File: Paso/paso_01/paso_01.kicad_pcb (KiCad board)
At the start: 2 copper layers, 97.4 x 87.2 mm, 2 parts

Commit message: Some minors update paso
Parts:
- removed the Ref** at (117.0, 110.7)
- added Ref**: Val**, paso_01:Maker_Lugo_100mm_02, F.Cu at (116.3, 122.3)
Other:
- board size 97.4 x 87.2 mm -> 97.4 x 87 mm

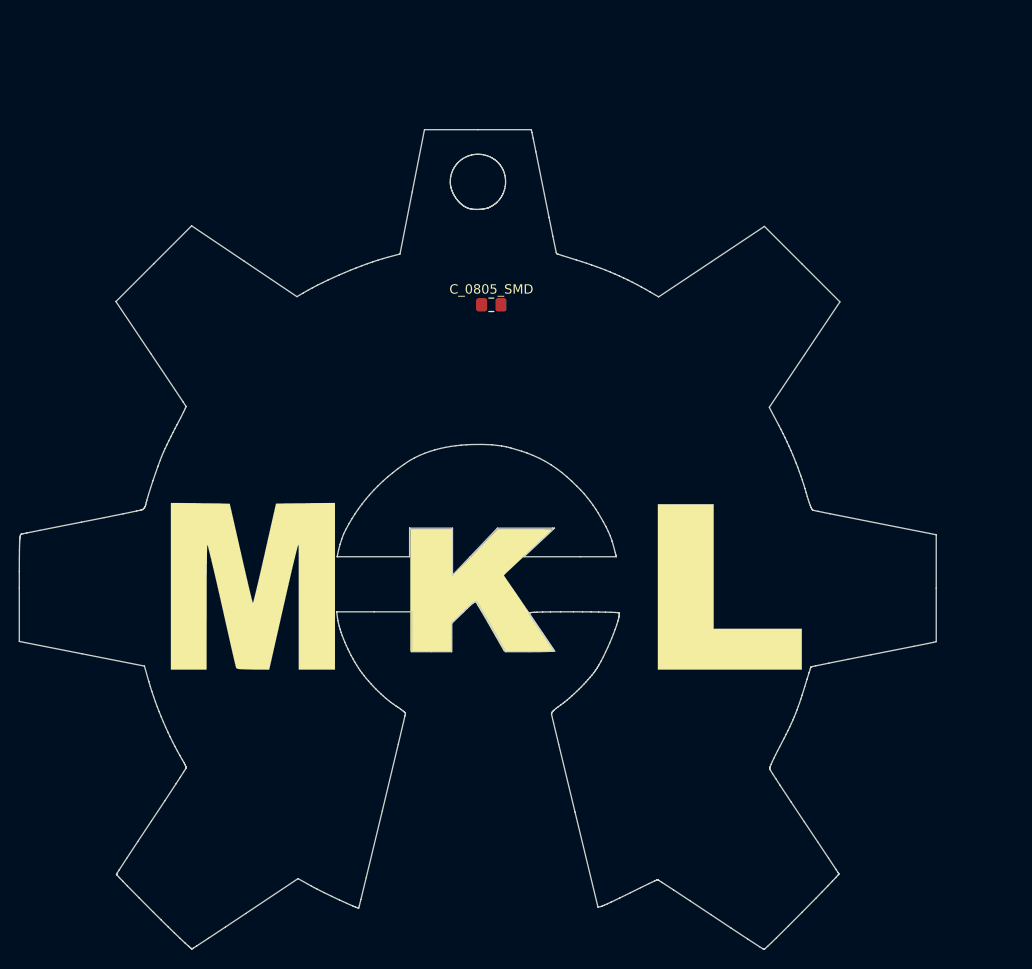
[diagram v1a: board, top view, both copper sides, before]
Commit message: Add ADC Nano
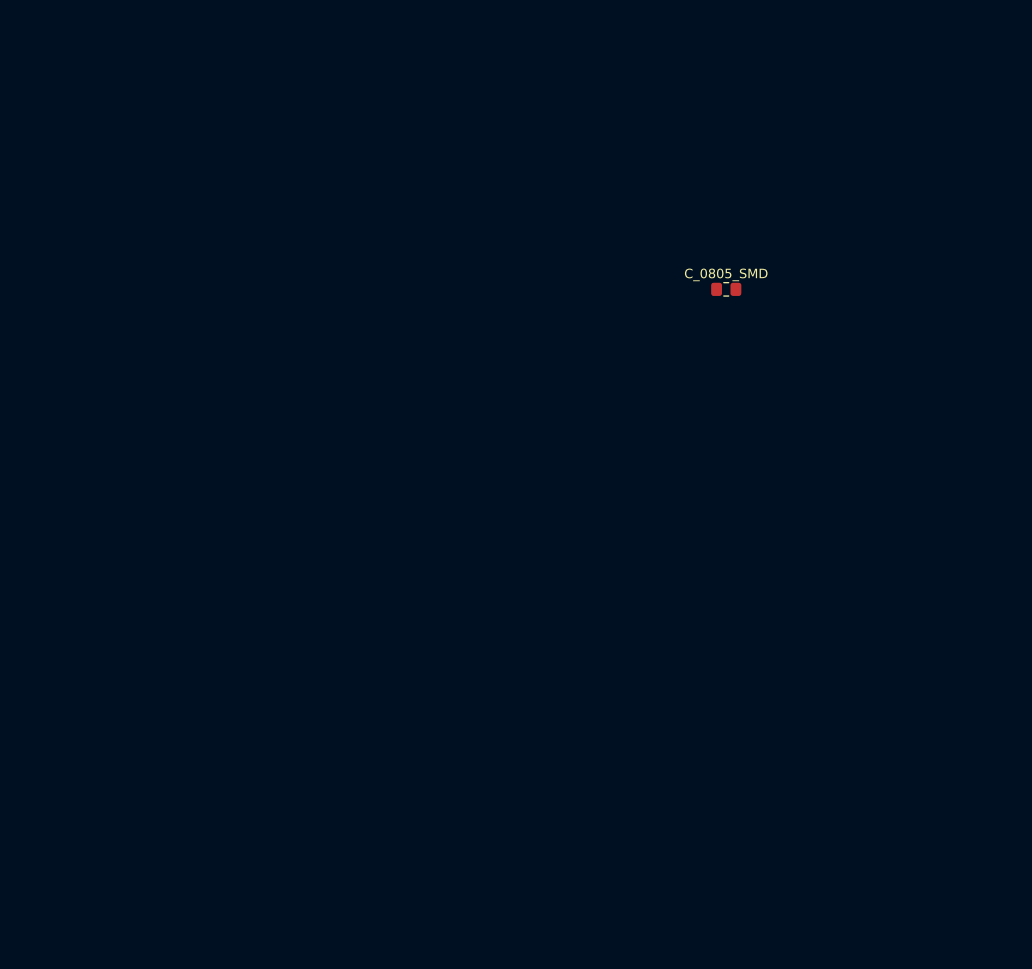
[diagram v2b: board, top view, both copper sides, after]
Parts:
- removed Ref**: Val**, paso_01:Maker_Lugo_100mm_02
- moved C_0805_SMD 25.0 mm to (141.7, 94.3)
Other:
- board outline removed

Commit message: Clear
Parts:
- added Ref**: Val**, paso_01:Maker_Lugo_60mm_03, F.Cu at (142.3, 104.5)
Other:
- board outline added: 59.5 x 53.3 mm
